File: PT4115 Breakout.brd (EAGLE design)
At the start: 48.3 x 48 mm, 31 parts

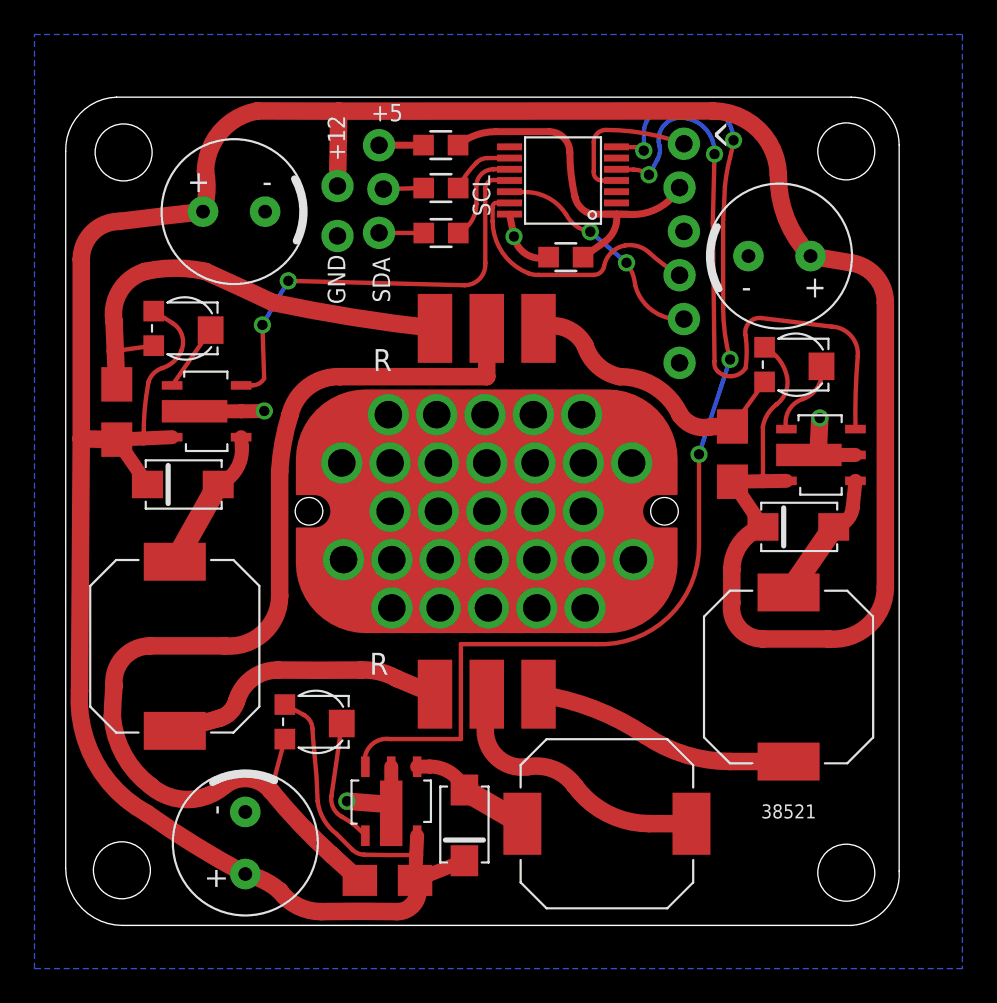
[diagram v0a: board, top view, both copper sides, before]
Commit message: Lots of minor tweaks
PIC programming header moved to get clearance around capacitor.
Some components moved to improve soldering ease.
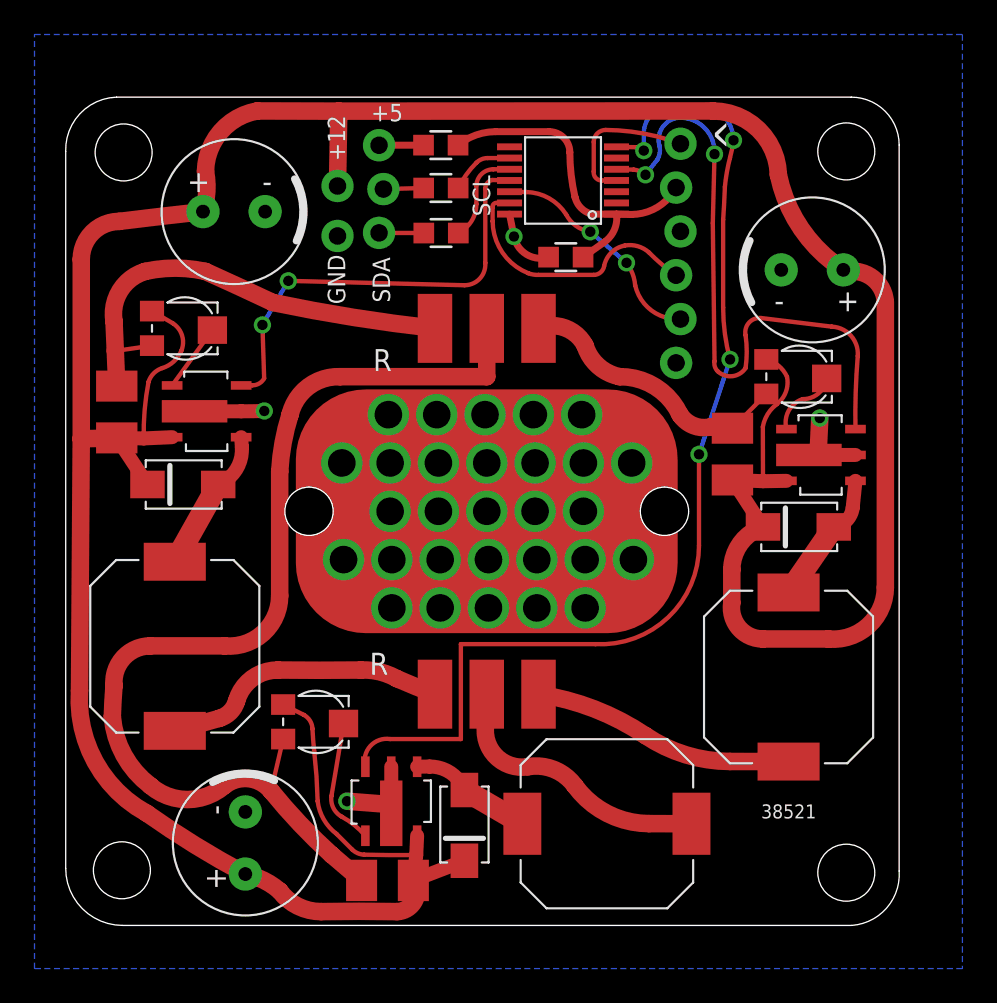
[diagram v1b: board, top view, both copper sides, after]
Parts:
- moved C9 2.06 mm to (43.3, 38.0)
- moved U$8 0.73 mm to (42.5, 31.8)
- moved JP3 0.20 mm to (35.5, 32.6)
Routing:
- net VIN: track 196.6 -> 195.9 mm
